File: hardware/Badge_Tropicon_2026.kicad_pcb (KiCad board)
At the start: 2 copper layers, 55 parts, among them J2 LCD, Q1 DMG3415U-7, U1 ESP32-S3-WROOM-1-N8, U2 BL8072CLTR33, U3 Si4463, U4 AHT30, U5 VGdd79S915N0S1, Y1 30MHz

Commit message: feat(Hw):Init_Floorplan
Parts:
- added J1: Battery, Footprints:BAT-TH_BH-AAA-A1AJ024, B.Cu at (127.4, 149.4)
- added P1: USB_C_Plug_USB2.0, Footprints:C393939, B.Cu at (194.1, 114.9)
- added Q2: BC846, Package_TO_SOT_SMD:SOT-23, B.Cu at (134.8, 106.4)
- added R13: 1K, Resistor_SMD:R_0603_1608Metric, B.Cu at (136.5, 103.9)
- added R14: 3.9r, Resistor_SMD:R_0603_1608Metric, B.Cu at (131.0, 106.4)
- added REF**: Display, Footprints:Display, F.Cu at (151.2, 107.8)
- added SW3: ON, Footprints:MSK12C02, B.Cu at (196.3, 135.9)
- AE1, AE2, C1, C12, C13, C14, C15, C16, C17, C18, C19, C2, C20, C21, C22, C3, C4, C5, C6, C7, D1, F1, J2, L1, L2, L3, Q1, R1, R10, R11, R12, R2, R3, R4, R5, R6, R7, R8, R9, SW1, SW2, U1, U2, U3, U4, U5, Y1: moved to B.Cu
- moved C6 156.6 mm to (188.3, 139.1), turned to -90 degrees
- moved SW5 155.3 mm to (166.7, 143.6), turned to 180 degrees
- moved U2 151.3 mm to (184.0, 141.5), turned to -90 degrees
- moved C7 149.2 mm to (182.8, 136.4), turned to 180 degrees
- moved SW6 148.9 mm to (151.2, 159.1), turned to 180 degrees
- moved SW2 143.6 mm to (169.1, 104.1)
- moved C21 142.0 mm to (195.7, 96.9), turned to -90 degrees
- moved F1 141.9 mm to (190.6, 118.5), turned to -90 degrees
- moved C9 140.4 mm to (161.8, 143.7), turned to 90 degrees
- moved R4 140.3 mm to (189.8, 123.6), turned to 180 degrees
- moved C18 139.7 mm to (191.2, 96.9), turned to -90 degrees
- moved R2 139.5 mm to (189.9, 116.2)
- moved R1 139.3 mm to (189.9, 113.4)
- moved C10 138.8 mm to (151.3, 155.3)
- moved L2 138.5 mm to (193.5, 96.1)
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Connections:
- J2 pad 8: GND -> /LEDK
- U1 pad 25: /IO0 -> /IO3
- U1 pad 26: /IO1 -> /IO2
- U1 pad 34: /IO2 -> /IO1
- U1 pad 35: /IO3 -> /IO0
- U1 pad 38: unconnected-(U1-IO2-Pad38) -> /LCD_BRIGHT
- Y1 pad 1: Net-(U3-XOUT) -> Net-(U3-XIN)
- Y1 pad 2: Net-(U3-XIN) -> GND
- Y1 pad 3: (no net) -> Net-(U3-XOUT)
- Y1 pad 4: (no net) -> GND
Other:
- board outline added: 99.7 x 100 mm

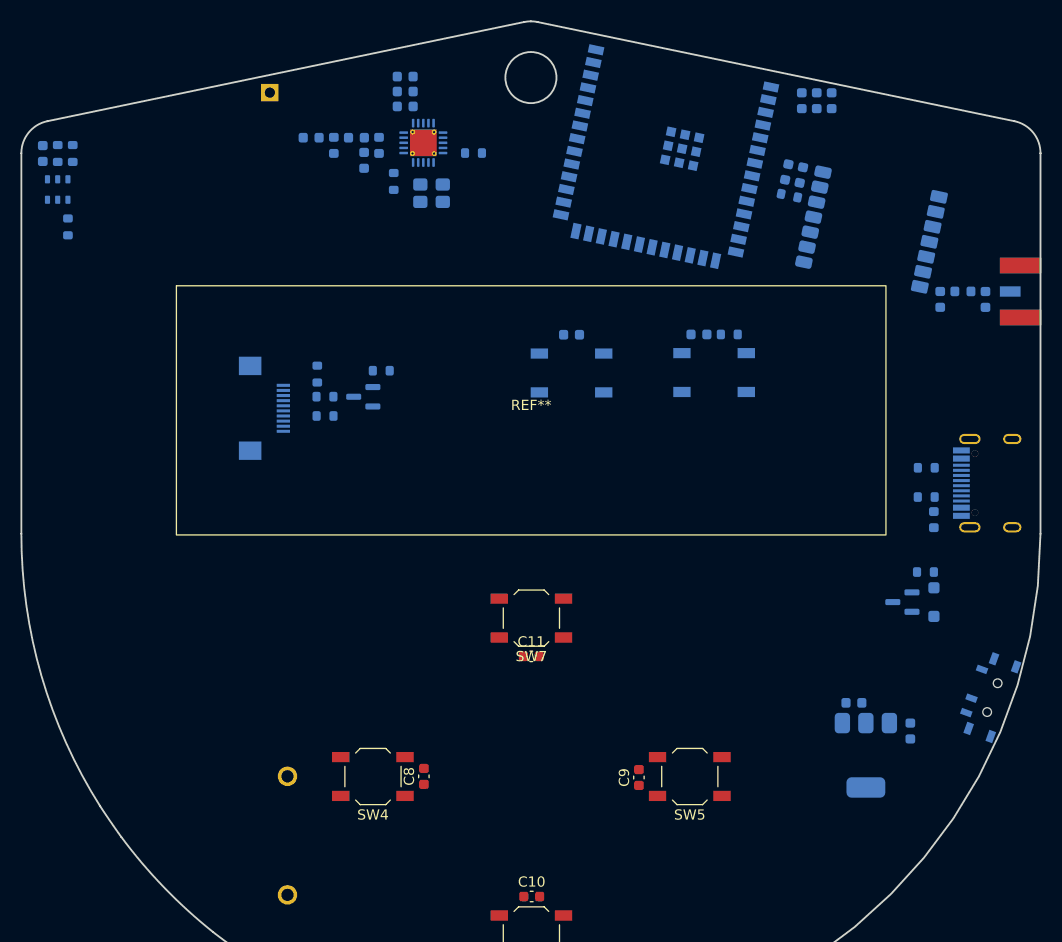
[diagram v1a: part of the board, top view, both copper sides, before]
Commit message: feat(Hw):Floorplan_Updated
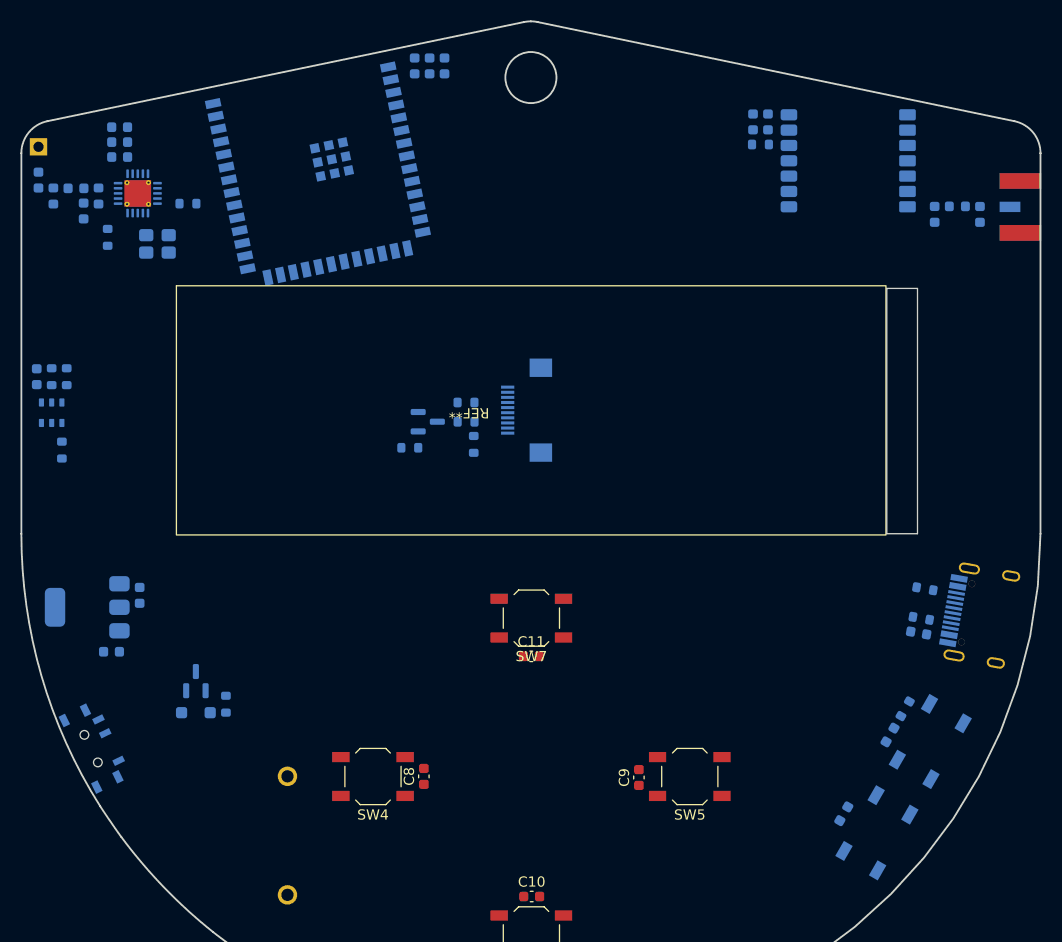
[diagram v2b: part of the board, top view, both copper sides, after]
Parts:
- moved SW3 88.3 mm to (108.2, 140.9), turned to 116 degrees
- moved C6 78.5 mm to (110.1, 131.4), turned to 180 degrees
- moved U2 77.6 mm to (107.8, 127.0), turned to 180 degrees
- moved D1 73.0 mm to (118.4, 137.3), turned to 0 degrees
- moved C7 70.7 mm to (112.9, 125.9), turned to 90 degrees
- moved R4 69.7 mm to (121.3, 136.5), turned to 90 degrees
- moved Q1 69.6 mm to (118.4, 134.3), turned to 90 degrees
- moved SW1 54.0 mm to (185.0, 149.1), turned to 60 degrees
- moved C4 53.9 mm to (181.8, 147.2), turned to 60 degrees
- moved C5 43.4 mm to (186.3, 139.5), turned to 60 degrees
- moved SW2 41.8 mm to (190.3, 140.2), turned to 60 degrees
- moved R5 40.5 mm to (187.8, 137.0), turned to 60 degrees
- moved C1 38.0 mm to (142.7, 74.1)
- moved C2 38.0 mm to (141.3, 74.1)
- moved C3 38.0 mm to (139.8, 74.1)
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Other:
- outline, holes or cut-outs redrawn

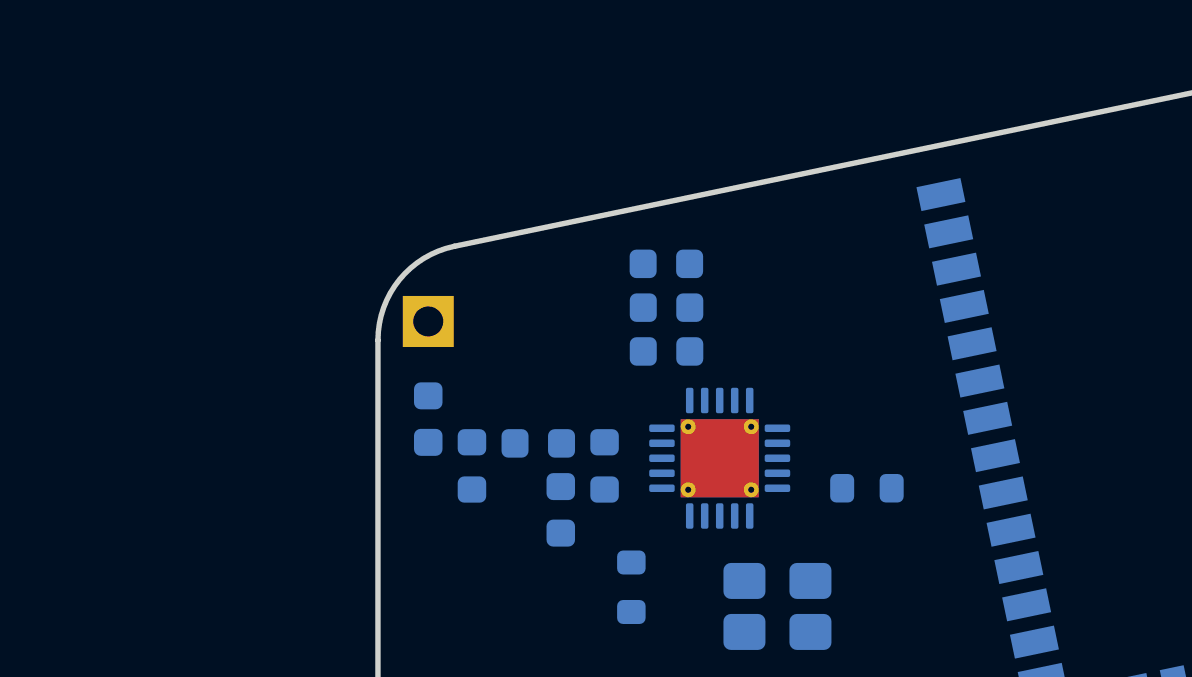
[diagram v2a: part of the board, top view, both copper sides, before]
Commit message: Fix: Modify RF filter and DNP
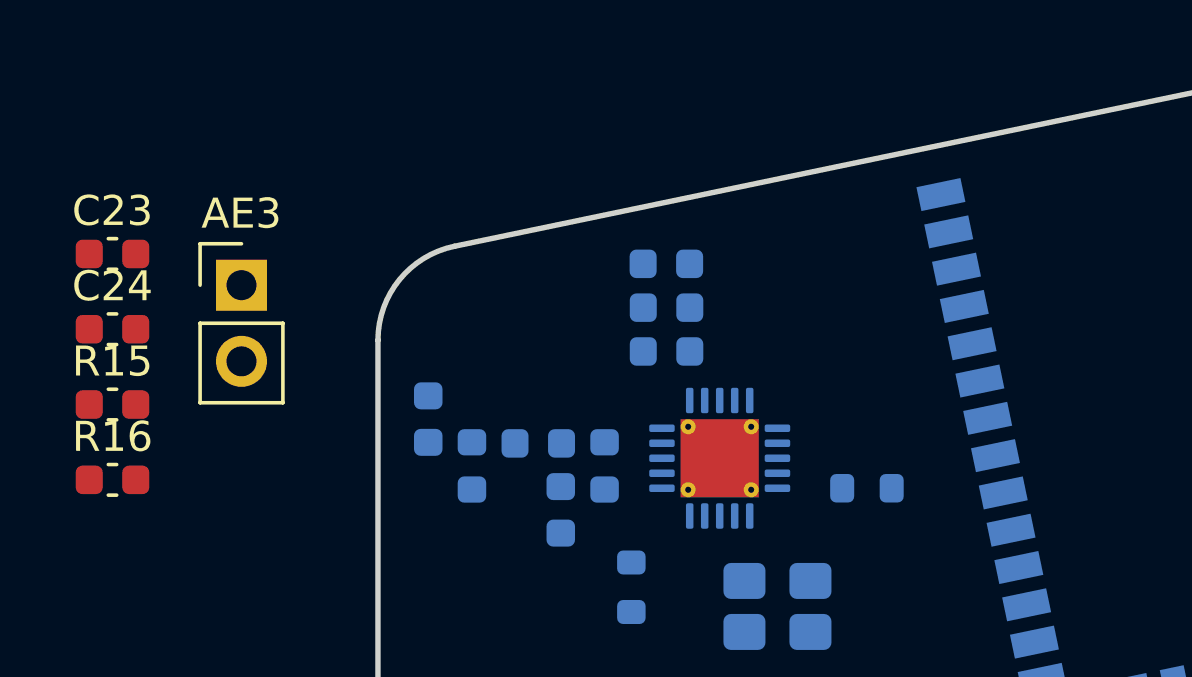
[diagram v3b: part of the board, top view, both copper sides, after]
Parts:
- removed AE2: Antenna, Connector_PinHeader_2.54mm:PinHeader_1x01_P2.54mm_Vertical
- added AE3: Antenna_Shield, Connector_PinHeader_2.54mm:PinHeader_1x02_P2.54mm_Vertical, F.Cu at (96.8, 80.8)
- added C23: 9pF, Capacitor_SMD:C_0603_1608Metric, F.Cu at (92.5, 79.7)
- added C24: 8.7pF, Capacitor_SMD:C_0603_1608Metric, F.Cu at (92.5, 82.2)
- added R15: 110r, Capacitor_SMD:C_0603_1608Metric, F.Cu at (92.5, 84.7)
- added R16: 113r, Capacitor_SMD:C_0603_1608Metric, F.Cu at (92.5, 87.2)

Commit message: feat(Hw):Update_Floorplan
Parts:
- removed C23: 9pF, Capacitor_SMD:C_0603_1608Metric
- AE3, C24, R15: moved to B.Cu
- R16: value 113r -> 0R; moved to B.Cu
- U2: footprint Package_TO_SOT_SMD:SOT-223-3_TabPin2 -> Package_TO_SOT_SMD:SOT-223
- moved R16 52.5 mm to (144.3, 78.8), turned to 90 degrees
- moved C24 51.4 mm to (143.5, 76.5), turned to 180 degrees
- moved R15 51.2 mm to (143.5, 81.0), turned to 180 degrees
- moved AE3 48.1 mm to (144.3, 73.2), turned to 90 degrees
- moved C22 40.6 mm to (143.5, 82.4), turned to 0 degrees
- moved C16 39.2 mm to (148.7, 90.4), turned to 90 degrees
- moved L3 37.6 mm to (142.0, 83.9), turned to 0 degrees
- moved C15 37.4 mm to (147.3, 90.4), turned to 90 degrees
- moved C20 36.1 mm to (142.7, 86.1), turned to 90 degrees
- moved C19 35.6 mm to (145.8, 90.4), turned to 90 degrees
- moved L1 33.1 mm to (142.0, 88.3), turned to 0 degrees
- moved C17 33.1 mm to (140.5, 86.8), turned to 0 degrees
- moved U3 30.0 mm to (142.2, 92.1), turned to -90 degrees
- moved R6 28.2 mm to (137.9, 89.2), turned to 180 degrees
- moved R7 25.5 mm to (141.2, 97.0), turned to -90 degrees
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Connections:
- R15 pad 1: Net-(C23-Pad2) -> Net-(C22-Pad2)
- R16 pad 1: Net-(C23-Pad2) -> Net-(C22-Pad2)
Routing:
- net +BATT: track 0.00 -> 28.5 mm, vias 0 -> 2
- net +3.3V: track 0.00 -> 21.1 mm
- net /UP: track 0.00 -> 12.8 mm
- net Net-(D1-K): track 0.00 -> 11.6 mm
- net /EN: track 0.00 -> 11.2 mm
- net /BOOT: track 0.00 -> 10.3 mm
- net /RIGHT: track 0.00 -> 9.11 mm
- net /LEFT: track 0.00 -> 8.95 mm
- net /DOWN: track 0.00 -> 8.93 mm
- net Net-(SW3-A): track 0.00 -> 8.05 mm
- net /D+: track 0.00 -> 6.96 mm
- net /D-: track 0.00 -> 6.84 mm
- net /Rxp: track 0.00 -> 6.64 mm
- net Net-(U3-XOUT): track 0.00 -> 5.38 mm
- net Net-(AE3-A): track 0.00 -> 4.78 mm
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
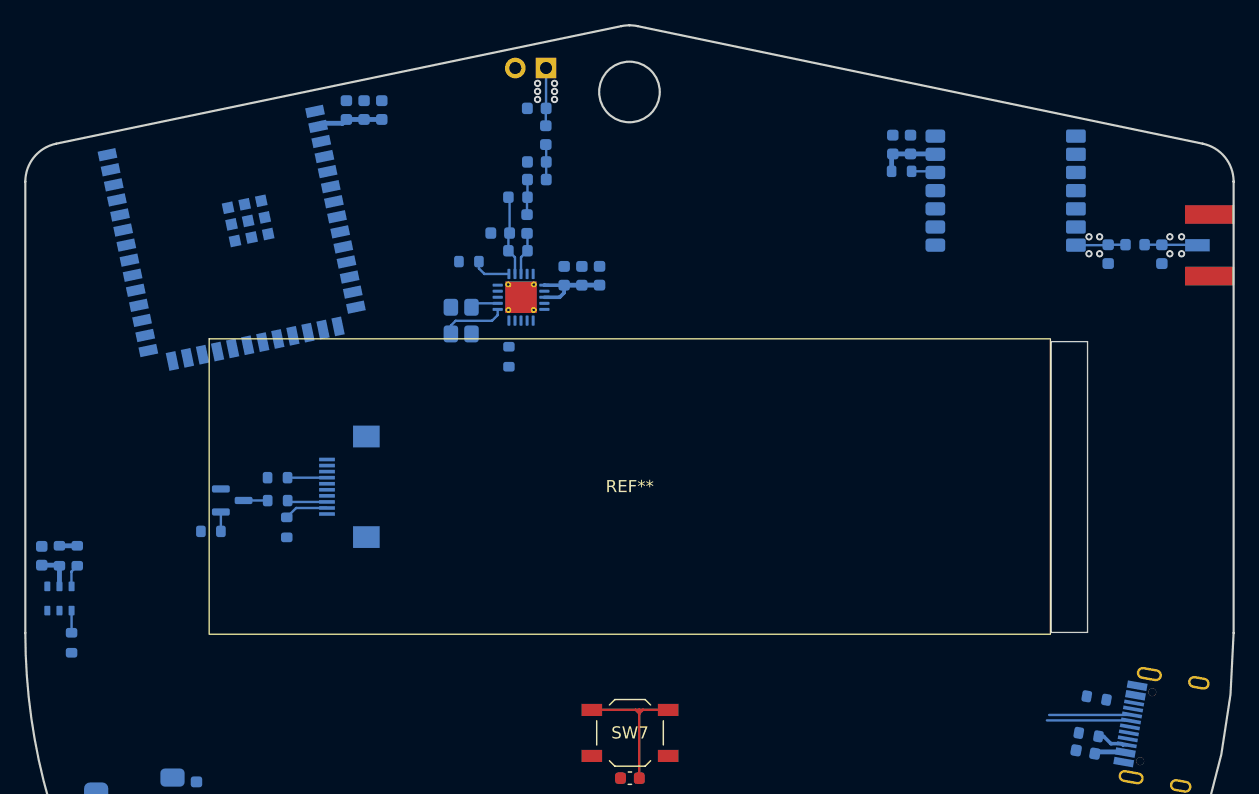
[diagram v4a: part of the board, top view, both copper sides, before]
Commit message: feat(Hw):Update_Schematic_And_Init_Route
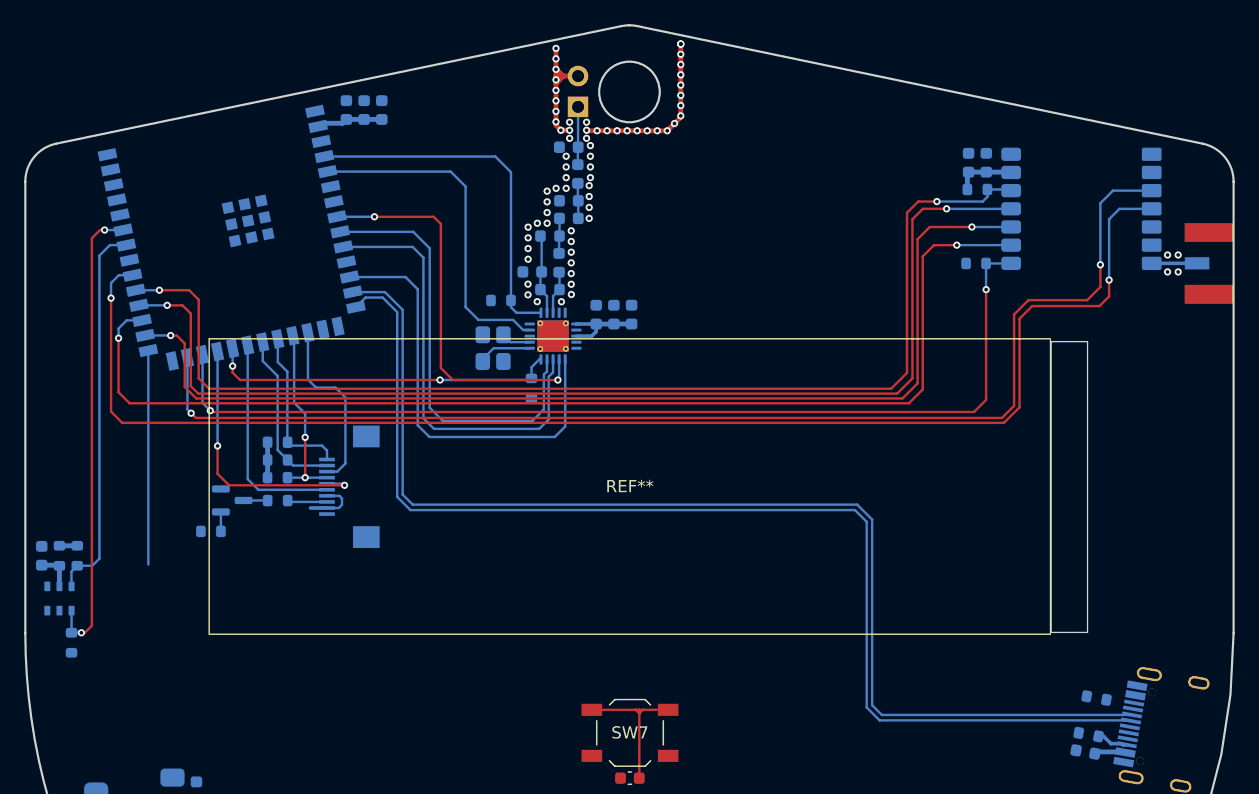
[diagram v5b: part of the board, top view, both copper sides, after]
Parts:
- removed C18, C21: 6.8pF, Capacitor_SMD:C_0603_1608Metric
- removed L2: 10nH, Inductor_SMD:L_0603_1608Metric
- added R17: 4.7K, Resistor_SMD:R_0603_1608Metric, B.Cu at (122.1, 104.1)
- added R18: 4.7K, Resistor_SMD:R_0603_1608Metric, B.Cu at (122.1, 105.6)
- R12: value 47r -> 10K
- moved R12 60.9 mm to (179.8, 89.3), turned to 180 degrees
- moved C12 6.43 mm to (180.6, 81.0)
- moved C13 6.43 mm to (179.2, 81.0)
- moved R8 6.43 mm to (179.9, 83.2)
- moved U5 6.43 mm to (188.5, 84.8)
- moved C16 4.16 mm to (151.4, 93.6)
- moved C17 4.16 mm to (143.2, 90.0)
- moved C20 4.16 mm to (145.4, 89.3)
- moved C22 4.16 mm to (146.2, 85.6)
- moved C24 4.16 mm to (146.2, 79.8)
- moved L1 4.16 mm to (144.6, 91.5)
- moved L3 4.16 mm to (144.6, 87.1)
- moved R15 4.16 mm to (146.2, 84.2)
- moved R6 4.16 mm to (140.6, 92.4)
- moved C15 4.16 mm to (149.9, 93.6)
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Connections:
- J2 pad 9: /LEDA -> +3.3V
- R12 pad 1: +3.3V -> /RST
- R12 pad 2: /LEDA -> +3.3V
- U1 pad 10: /MISO -> /MISO2
- U1 pad 11: /SCK -> /RIGHT
- U1 pad 12: /RSTB -> /IRQ
- U1 pad 15: /RST -> unconnected-(U1-IO3-Pad15)
- U1 pad 16: /BUSY -> unconnected-(U1-IO46-Pad16)
- U1 pad 21: /LEFT -> /TE
- U1 pad 22: /RIGHT -> /CS2
- U1 pad 23: /DOWN -> /RSTB
- U1 pad 24: /UP -> /RST
- U1 pad 25: /IO3 -> /DIO
- U1 pad 26: /IO2 -> unconnected-(U1-IO45-Pad26)
- U1 pad 28: /MOSI2 -> /MOSI
- U1 pad 29: /MISO2 -> /MISO
- U1 pad 30: /SCK2 -> /SCK
- U1 pad 31: /CS2 -> /CS0
- U1 pad 32: /IRQ -> /BUSY
- U1 pad 33: /SDN -> /UP
- U1 pad 34: /IO1 -> /SCL1
- U1 pad 35: /IO0 -> /SDA1
- U1 pad 37: unconnected-(U1-TXD0-Pad37) -> /DOWN
- U1 pad 39: unconnected-(U1-IO1-Pad39) -> /LEFT
- U1 pad 4: /DIO -> /SDN
- U1 pad 5: /SDA1 -> /IO2
- U1 pad 6: /SCL1 -> /IO1
- U1 pad 7: /TE -> /IO0
- U1 pad 8: /CS0 -> /SCK2
- U1 pad 9: /MOSI -> /MOSI2
- U3 pad 20: /IO3 -> unconnected-(U3-GPIO3-Pad20)
- U5 pad 14: Net-(U5-ANT) -> Net-(AE1-A)
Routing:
- net /BUSY: track 0.00 -> 114.3 mm, vias 0 -> 2
- net /DIO: track 0.00 -> 100.4 mm, vias 0 -> 2
- net /MISO: track 0.00 -> 93.4 mm, vias 0 -> 2
- net /SCK: track 0.00 -> 92.5 mm, vias 0 -> 2
- net /CS0: track 2.00 -> 94.4 mm, vias 0 -> 2
- net /D-: track 6.84 -> 96.7 mm
- net /D+: track 6.96 -> 96.7 mm
- net /MOSI: track 0.00 -> 88.6 mm, vias 0 -> 2
- net /RST: track 0.00 -> 82.7 mm, vias 0 -> 2
- net /SDA1: track 1.83 -> 38.6 mm, vias 0 -> 2
- net /MISO2: track 0.00 -> 36.4 mm
- net /IRQ: track 0.00 -> 35.7 mm
- net /MOSI2: track 0.00 -> 35.6 mm
- net /SCK2: track 0.00 -> 32.5 mm, vias 0 -> 2
- net /SCL1: track 1.90 -> 31.6 mm
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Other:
- board text added: "${REFERENCE}"

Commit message: feat(Hw):Update_Route
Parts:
- moved Y1 0.12 mm to (139.9, 96.2)
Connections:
- U1 pad 6: /IO1 -> /IO0
- U1 pad 7: /IO0 -> /IO1
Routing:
- net +3.3V: track 28.6 -> 336.1 mm, vias 0 -> 15
- net /EN: track 11.2 -> 130.2 mm, vias 0 -> 2
- net /RIGHT: track 9.11 -> 122.7 mm, vias 0 -> 3
- net /DOWN: track 8.93 -> 118.6 mm, vias 0 -> 1
- net /BOOT: track 27.9 -> 128.0 mm
- net /LEFT: track 8.95 -> 101.5 mm, vias 0 -> 1
- net VBUS: track 3.88 -> 79.3 mm, vias 0 -> 2
- net /UP: track 12.8 -> 86.6 mm, vias 0 -> 1
- net /IO0: track 0.00 -> 43.9 mm, vias 0 -> 2
- net /IO1: track 0.00 -> 38.3 mm, vias 0 -> 2
- net /LCD_BRIGHT: track 0.00 -> 34.4 mm, vias 0 -> 2
- net Net-(F1-Pad1): track 2.57 -> 10.6 mm
- net /D-: track 96.7 -> 100.5 mm
- net /D+: track 96.7 -> 100.1 mm
- net GND: track 25.5 -> 28.7 mm, vias 70 -> 121
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- added copper zone on B.Cu, net GND
- added copper zone on F.Cu, net GND
